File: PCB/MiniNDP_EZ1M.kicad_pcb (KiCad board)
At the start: 2 copper layers, 60 x 34 mm, 19 parts, among them J1 Conn_02x20_Odd_Even, U1 AS6C8008_TSOPII, U2 HC238, U3 4040, U4 FCT841

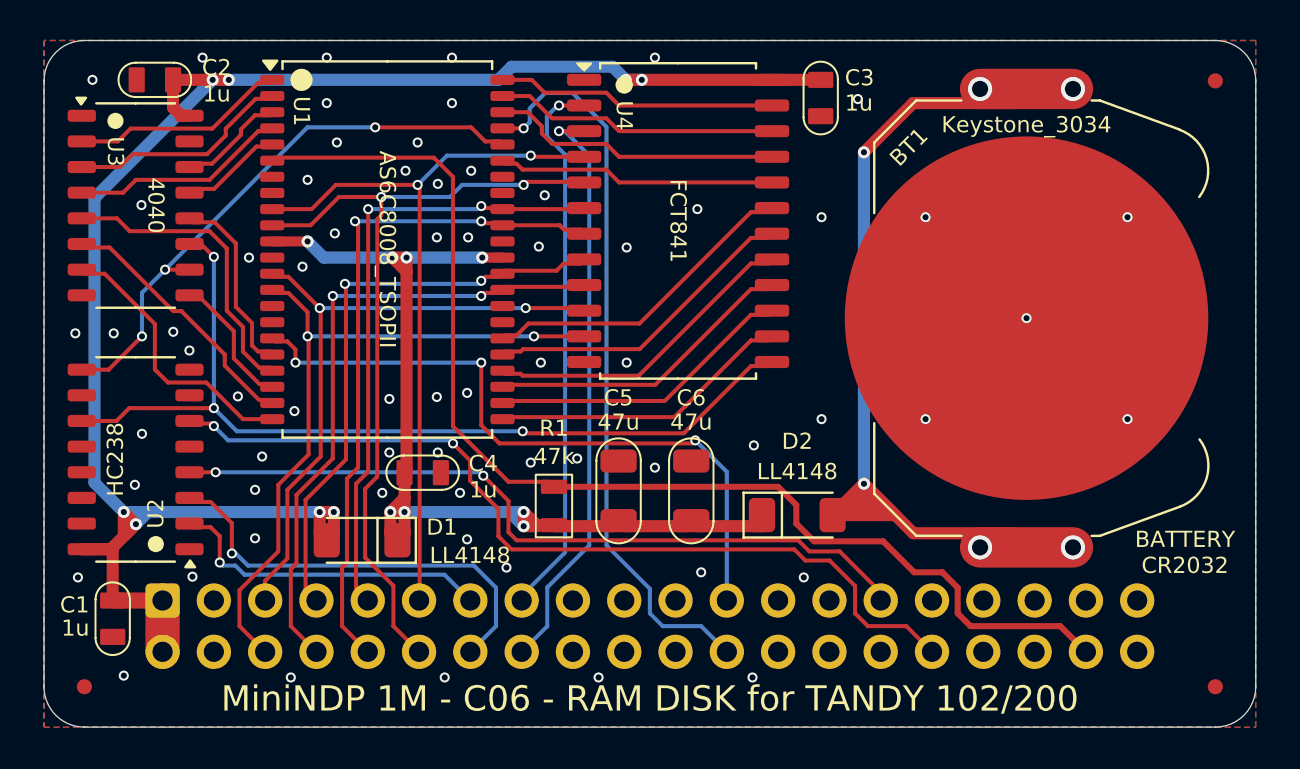
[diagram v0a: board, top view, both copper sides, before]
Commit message: add SL1M, rename 1M_C to EZ1M, remove 256_F & 512_F from readme
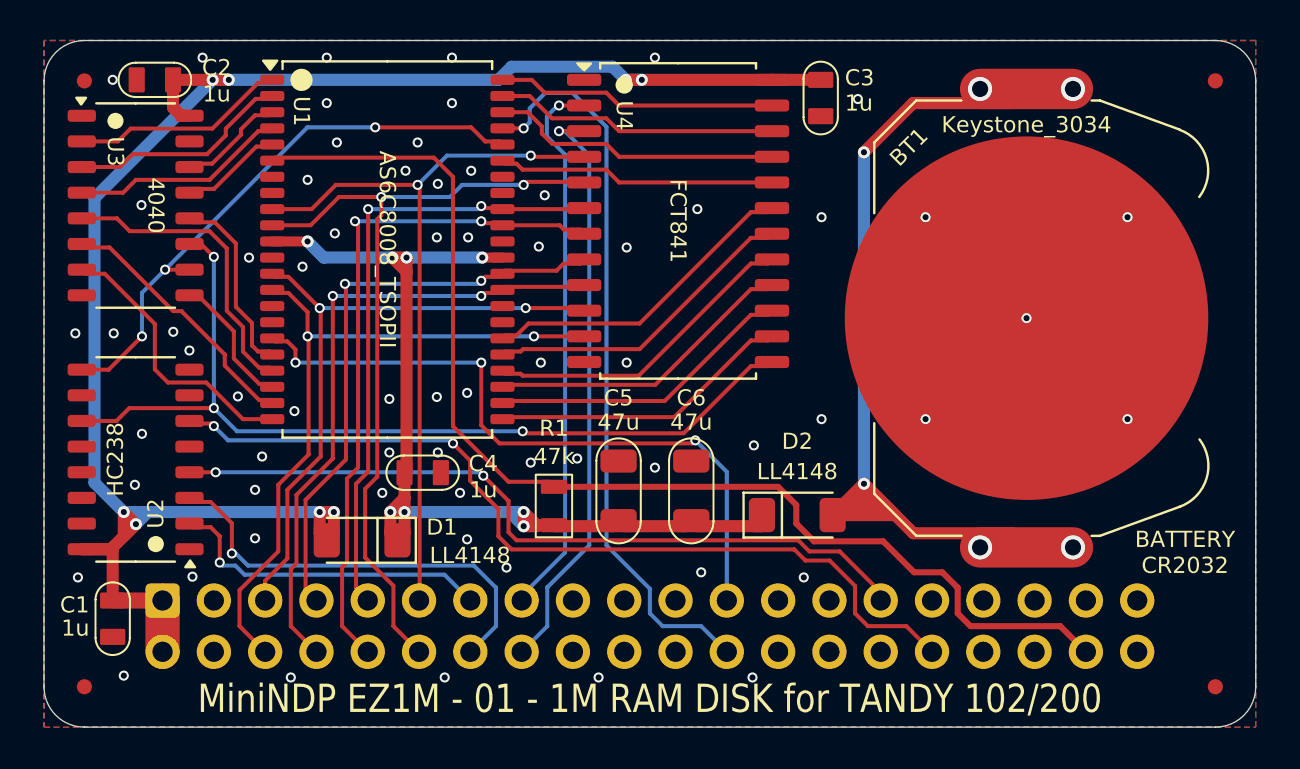
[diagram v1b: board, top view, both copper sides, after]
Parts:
- added F3: Fiducial_0.75_1.5, 000_LOCAL:Fiducial_0.75_1.5, F.Cu at (124.0, 88.0)
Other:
- board text added: "${TITLE} - ${REVISION} - 1M RAM DISK for TANDY 102/200"
- board text added: "100 1 CLEAR0,61558:T=61558:E=62957:OUT129,2 200 1 CLEAR0,59715:T=59715:E=61101:OUT129,2 2 FORA=0TO15:N=INP(131):NEXT:FORA=TTOE 3 POKEA,INP(131):IFA=T+1007THENOUT129,1 4 ?{dblquote}.{dblquote};:NEXT:SAVEM{dblquote}RAMDSK{dblquote},T,E,T"
- board text added: "1M RAM DISK for TANDY 102/200"
- board text added: "BANK0: OUT 129,N BANK1: OUT 133,N BANK2: OUT 137,N BANK3: OUT 141,N"
- board text added: "Bootstrap RAMDSK from BANK 0. For BANK 1 change OUT129 to OUT133. RAM100.CO or RAM200.CO must be the first file in the bank."
- board text added: "Use ENIG copper finish for gold battery contact."
- board text removed: "${TITLE} - ${REVISION} - RAM DISK for TANDY 102/200"
- board text removed: "OUT X%,N% N% = INP(131) OUT 131,N%"
- board text removed: "RAM DISK for TANDY 102/200"
- board text removed: "Select bank X%, block N%, offset 0 Read byte & advance offset Write byte & advance offset"
- board text removed: "Use ENIG copper finish for gold battery terminal."
- board text removed: "X% : 129=BANK0 133=BANK1 137=BANK2 141=BANK3 N% : 0-255 offset counts 0-1023"
